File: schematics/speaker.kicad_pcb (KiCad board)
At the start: 2 copper layers, 49 x 26.2 mm, 20 parts, among them IC1 MCP73833-AMI_UN, IC2 AZ1117CR-3.3TRG1, IC3 MAX98357AGTE_V+T, J1 Conn_01x02_Male, J2 Conn_01x04, J3 USB_B_Micro, J4 Conn_01x02, J5 Conn_01x02, J6 Conn_01x02, U1 ESP32-C3-WROOM-02

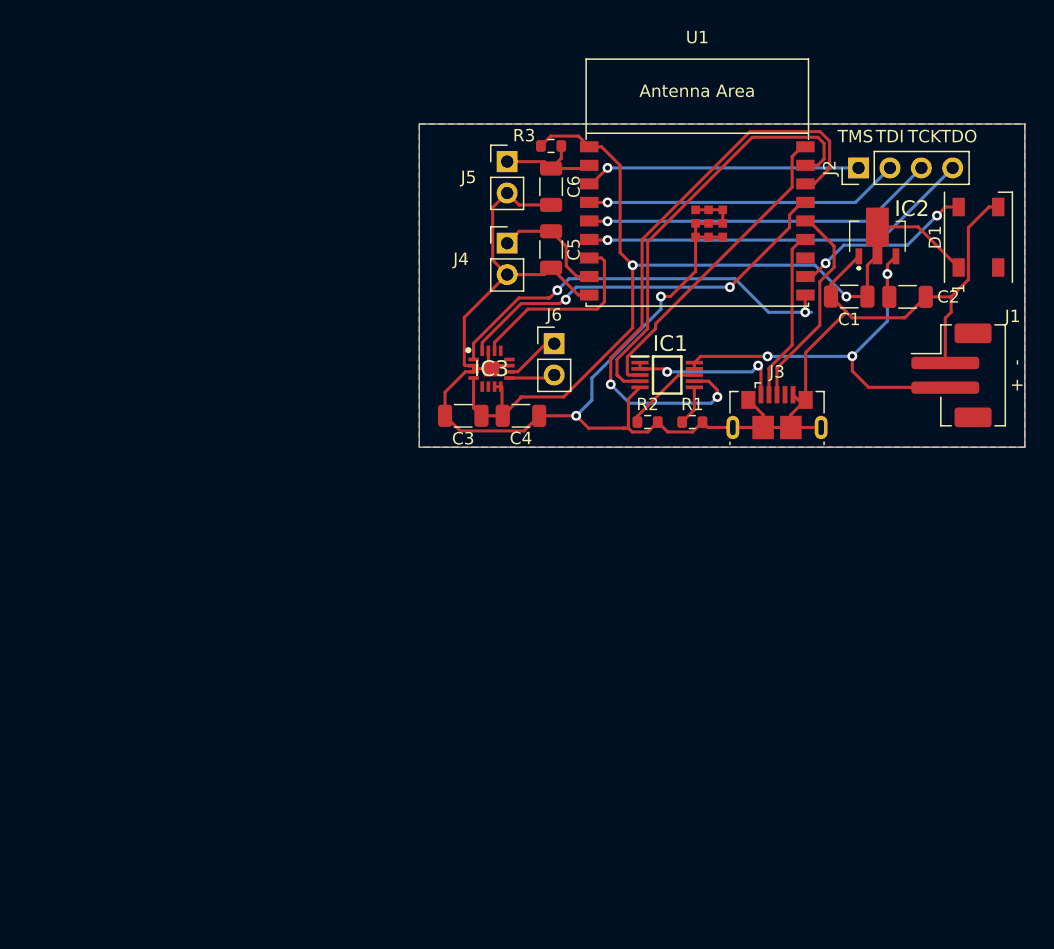
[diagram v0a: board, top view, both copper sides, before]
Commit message: Updated to kicad 6. Added mounting hole. Corrected battery management design
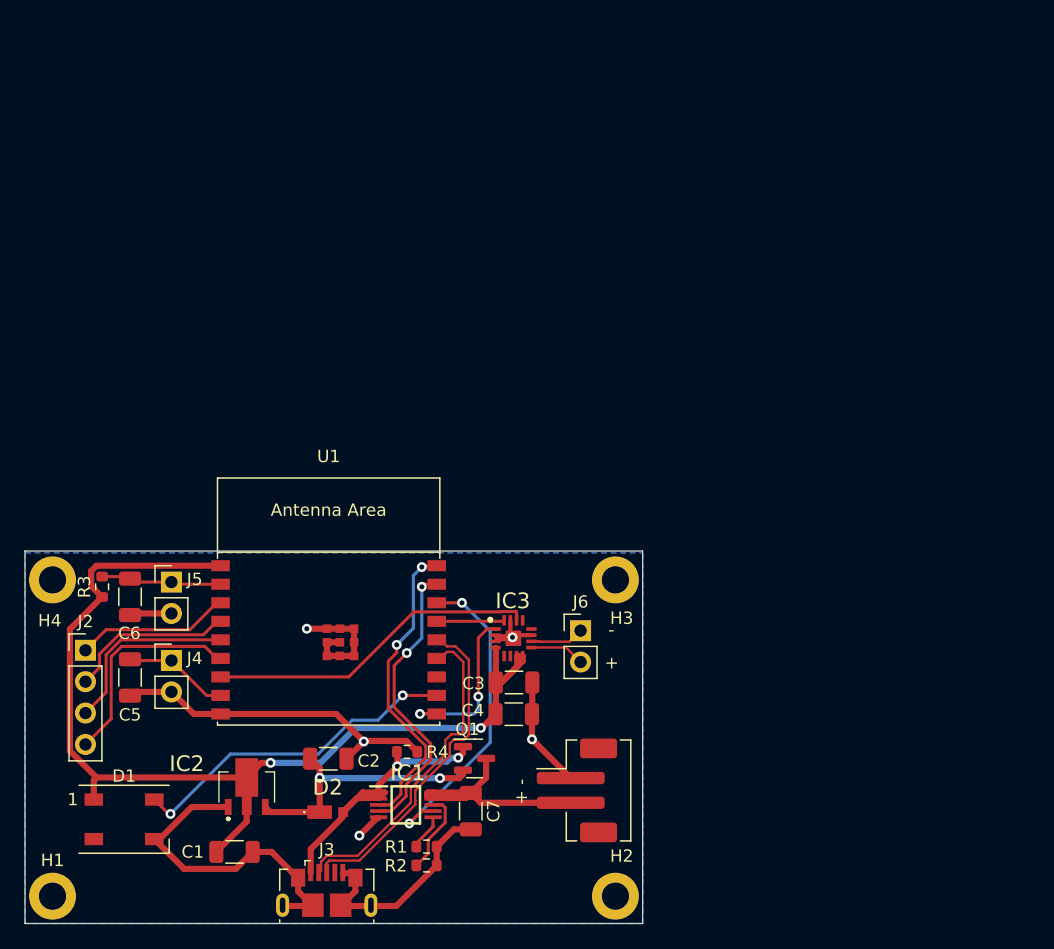
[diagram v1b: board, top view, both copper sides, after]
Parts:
- removed J1: Conn_01x02_Male, Connector_JST:JST_PH_B2B-PH-SM4-TB_1x02-1MP_P2.00mm_Vertical
- added + -: Conn_01x02_Male, Connector_JST:JST_PH_B2B-PH-SM4-TB_1x02-1MP_P2.00mm_Vertical, F.Cu at (134.7, 119.2)
- added C7: 4.7uF, Capacitor_SMD:C_1206_3216Metric, F.Cu at (126.1, 120.9)
- added D2: PD3S230H-7, lib:PD3S230H7, F.Cu at (114.7, 121.0)
- added H1: MountingHole, MountingHole:MountingHole_2.2mm_M2_DIN965_Pad, F.Cu at (92.2, 127.8)
- added H2: MountingHole, MountingHole:MountingHole_2.2mm_M2_DIN965_Pad, F.Cu at (137.8, 127.8)
- added H3: MountingHole, MountingHole:MountingHole_2.2mm_M2_DIN965_Pad, F.Cu at (137.8, 102.2)
- added H4: MountingHole, MountingHole:MountingHole_2.2mm_M2_DIN965_Pad, F.Cu at (92.2, 102.2)
- added Q1: DMG2301L, Package_TO_SOT_SMD:SOT-23, F.Cu at (126.4, 116.6)
- added R4: 10K, Resistor_SMD:R_0603_1608Metric, F.Cu at (120.9, 116.1)
- IC1: footprint SamacSys_Parts:SOP50P490X110-10N -> lib:SOP50P490X110-10N
- IC2: footprint SamacSys_Parts:AZ1117CR33TRG1 -> lib:AZ1117CR33TRG1
- IC3: footprint SamacSys_Parts:QFN50P300X300X80-17N -> lib:QFN50P300X300X80-17N
- moved D1 83.7 mm to (98.0, 121.6), turned to 0 degrees
- moved J2 73.8 mm to (94.9, 107.9), turned to 0 degrees
- moved IC2 67.8 mm to (108.0, 117.7)
- moved C1 67.1 mm to (107.0, 124.2), turned to 0 degrees
- moved C2 60.0 mm to (114.6, 116.7)
- moved J3 53.1 mm to (114.4, 127.3)
- moved R3 50.9 mm to (96.2, 102.7), turned to 90 degrees
- moved C5 48.6 mm to (98.5, 110.1)
- moved C6 47.6 mm to (98.5, 103.6)
- moved U1 45.2 mm to (114.6, 105.2)
- moved J5 43.6 mm to (101.9, 102.4)
- moved J4 43.4 mm to (101.9, 108.7)
- moved IC1 40.7 mm to (120.8, 120.4)
- moved R1 40.5 mm to (122.5, 123.8)
- moved R2 40.1 mm to (122.5, 125.3)
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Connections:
- C2 pad 1: /power/VBAT -> VCC
- D1 pad 2: Net-(D1-Pad2) -> unconnected-(D1-Pad2)
- IC2 pad 3: /power/VBAT -> VCC
- IC3 pad 12: Net-(IC3-Pad12) -> unconnected-(IC3-Pad12)
- IC3 pad 13: Net-(IC3-Pad13) -> unconnected-(IC3-Pad13)
- IC3 pad 5: Net-(IC3-Pad5) -> unconnected-(IC3-Pad5)
- IC3 pad 6: Net-(IC3-Pad6) -> unconnected-(IC3-Pad6)
- J3 pad 4: Net-(J3-Pad4) -> unconnected-(J3-Pad4)
- U1 pad 12: Net-(U1-Pad12) -> unconnected-(U1-Pad12)
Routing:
- net GND: track 152.6 -> 102.2 mm, vias 2 -> 5
- net /audio/BCLK: track 32.1 -> 5.49 mm, vias 2 -> 0
- net /comm/PG: track 48.8 -> 25.9 mm
- net VCC: track 0.00 -> 21.2 mm, vias 0 -> 2
- net /audio/DATA: track 33.4 -> 13.7 mm
- net /power/VBAT: track 36.9 -> 19.7 mm, vias 3 -> 0
- net /comm/TDO: track 31.9 -> 17.6 mm, vias 1 -> 0
- net /comm/TCK: track 28.7 -> 15.2 mm, vias 1 -> 0
- net /comm/D-: track 14.0 -> 26.6 mm
- net Net-(D1-Pad4): track 14.7 -> 27.3 mm
- net /comm/TDI: track 25.5 -> 13.6 mm, vias 1 -> 0
- net /audio/LRCLK: track 15.6 -> 26.8 mm
- net /comm/STAT2: track 34.6 -> 23.9 mm, vias 0 -> 2
- net VBUS: track 13.3 -> 23.9 mm
- net /comm/D+: track 17.1 -> 27.2 mm
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- removed copper zone on F.Cu, net GND
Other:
- board size 49 x 26.2 mm -> 50 x 30.2 mm
- net class Default removed
- board text removed: "TCK"
- board text removed: "TDI"
- board text removed: "TDO"
- board text removed: "TMS"
